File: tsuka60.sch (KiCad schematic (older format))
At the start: 165 parts, among them SW1 SW_Push, U1 ATmega32U4-AU, Y1 Resonator_Small

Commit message: completed all traces
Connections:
- net Col3: now also U1.31 (PC6); no longer U1.32 (PC7)
- net Col4: now also U1.32 (PC7); no longer U1.31 (PC6)
- net Row3: now also U1.29 (PB5); no longer U1.28 (PB4)
- net Row4: now also U1.28 (PB4); no longer U1.29 (PB5)
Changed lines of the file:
@@
 Text GLabel 5750 12050 2    50   Input ~ 0
 Row2
+Text GLabel 5750 10850 2    50   Input ~ 0
+Row3
 Text GLabel 5750 10750 2    50   Input ~ 0
-Row3
-Text GLabel 5750 10850 2    50   Input ~ 0
 Row4
 Text GLabel 5750 12750 2    50   Input ~ 0
@@
 Text GLabel 5750 12950 2    50   Input ~ 0
 Col2
+Text GLabel 5750 11250 2    50   Input ~ 0
+Col3
 Text GLabel 5750 11350 2    50   Input ~ 0
-Col3
-Text GLabel 5750 11250 2    50   Input ~ 0
 Col4
 Text GLabel 5750 13250 2    50   Input ~ 0

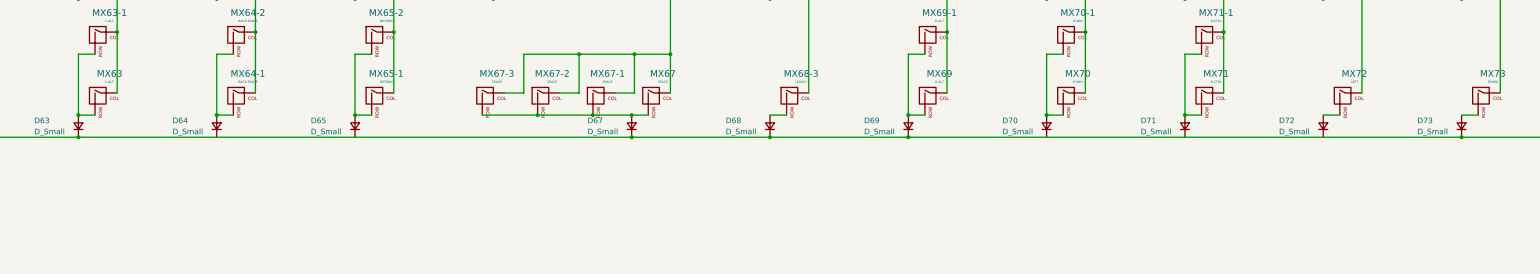
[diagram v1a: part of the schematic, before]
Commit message: Fixed broken traces
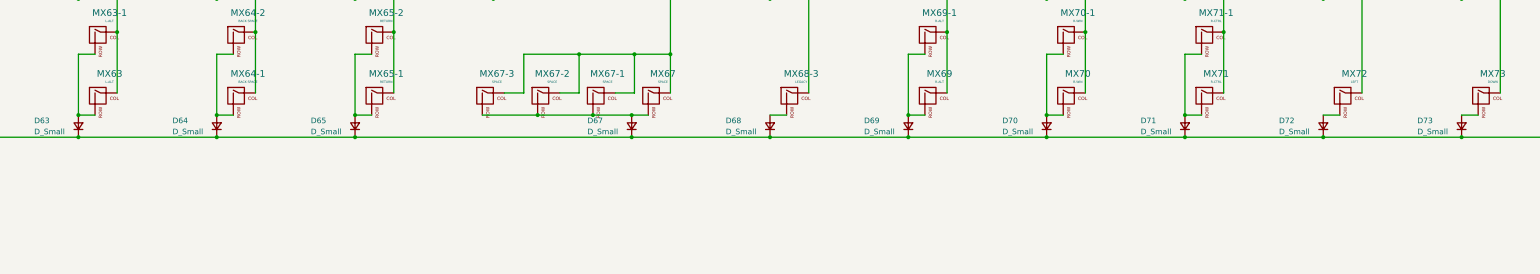
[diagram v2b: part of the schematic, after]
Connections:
- net Row4: now also D64.1 (K), D65.1 (K), D70.1 (K), D71.1 (K), D72.1 (K)
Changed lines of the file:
@@
 Wire Wire Line
 	18800 7300 18650 7300
-Wire Wire Line
-	18650 7500 19900 7500
 Connection ~ 18650 7500
 $Comp
@@
 	8650 6250 11150 6250
 Wire Wire Line
-	4900 7500 9900 7500
-Wire Wire Line
-	12400 7500 17400 7500
-Wire Wire Line
 	17750 5850 17750 7100
 Wire Wire Line
@@
 	16500 1250 16500 2100
 Connection ~ 16500 2100
+Wire Wire Line
+	4900 7500 6150 7500
+Connection ~ 6150 7500
+Wire Wire Line
+	6150 7500 7400 7500
+Connection ~ 7400 7500
+Wire Wire Line
+	7400 7500 9900 7500
+Wire Wire Line
+	18650 7500 19900 7500
+Wire Wire Line
+	12400 7500 13650 7500
+Connection ~ 13650 7500
+Wire Wire Line
+	13650 7500 14900 7500
+Connection ~ 16150 7500
+Wire Wire Line
+	16150 7500 17400 7500
+Connection ~ 14900 7500
+Wire Wire Line
+	14900 7500 16150 7500
 $EndSCHEMATC

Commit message: updated the schematic
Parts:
- removed D68: D_Small, Diode_SMD:D_0805_2012Metric, symbol Device:D_Small
- removed MX67-1: SPACE, MX_Alps_Hybrid:MX-2.75U-ReversedStabilizers-NoLED, symbol MX_Alps_Hybrid:MX-NoLED
- removed MX67-2: SPACE, MX_Alps_Hybrid:MX-3U-ReversedStabilizers-NoLED, symbol MX_Alps_Hybrid:MX-NoLED
- removed MX67-3: SPACE, MX_Alps_Hybrid:MX-6.25U-ReversedStabilizers-NoLED, symbol MX_Alps_Hybrid:MX-NoLED
- removed MX68-3: LEGACY, MX_Alps_Hybrid:MX-1.25U-NoLED, symbol MX_Alps_Hybrid:MX-NoLED
- added D37, D39, D52, D54, D66: D_Small, Diode_SMD:D_0805_2012Metric, symbol Device:D_Small
- added MX31-1: CAPS-SHORT, MX_Alps_Hybrid:MX-1.25U-NoLED, symbol MX_Alps_Hybrid:MX-NoLED
- added MX37: LEGACY-H, MX_Alps_Hybrid:MX-1U-NoLED, symbol MX_Alps_Hybrid:MX-NoLED
- added MX39: H, MX_Alps_Hybrid:MX-1.5U-NoLED, symbol MX_Alps_Hybrid:MX-NoLED
- added MX44-1: RETURN-SHORT, MX_Alps_Hybrid:MX-1.75U-NoLED, symbol MX_Alps_Hybrid:MX-NoLED
- added MX52: M1, MX_Alps_Hybrid:MX-1U-NoLED, symbol MX_Alps_Hybrid:MX-NoLED
- added MX54: M3, MX_Alps_Hybrid:MX-1U-NoLED, symbol MX_Alps_Hybrid:MX-NoLED
- added MX65-2: RETURN, MX_Alps_Hybrid:MX-1.5U-NoLED, symbol MX_Alps_Hybrid:MX-NoLED
- added MX65-3: SPACE, MX_Alps_Hybrid:MX-1.5U-NoLED, symbol MX_Alps_Hybrid:MX-NoLED
- added MX66-1, MX66-2: SPACE RIGHT, MX_Alps_Hybrid:MX-1.5U-NoLED, symbol MX_Alps_Hybrid:MX-NoLED
- MX1: value MX-LED -> ESC
- MX10: value MX-LED -> 7
- MX11: value MX-LED -> 8
- MX12: value MX-LED -> 9
- MX13: value MX-LED -> 10
- MX14: value MX-LED -> MINUS
- MX15: value MX-LED -> PLUS
- MX16: value MX-LED -> TAB 1
- MX17: value MX-LED -> TAB 2
- MX18: value MX-LED -> Q
- MX19: value MX-LED -> W
- MX2: value MX-LED -> TILDE
- MX20: value MX-LED -> E
- MX21: value MX-LED -> R
- MX22: value MX-LED -> T
- MX23: value MX-LED -> M4
- MX24: value MX-LED -> Y
- MX25: value MX-LED -> U
- MX26: value MX-LED -> I
- MX27: value MX-LED -> O
- MX28: value MX-LED -> P
- MX29: value MX-LED -> L-BRACKET
- MX3: value MX-LED -> 1
- MX30: value MX-LED -> R-BRACKET
- MX31: value MX-LED -> CAPS
- MX32: value MX-LED -> A
- MX33: value MX-LED -> S
- MX34: value MX-LED -> D
- MX35: value MX-LED -> F
- MX36: value MX-LED -> G
- MX38: value MX-LED -> BACKSPACE
- MX4: value MX-LED -> 2
- MX40: value MX-LED -> J
- MX41: value MX-LED -> K
- MX42: value MX-LED -> L
- MX43: value MX-LED -> SEMI-COLON
- MX44: value MX-LED -> RETURN
- MX45: value MX-LED -> BACKSPACE 2U
- MX46: value MX-LED -> L-SHIFT
- MX47: value MX-LED -> Z
- MX48: value MX-LED -> X
- MX49: value MX-LED -> C
- MX5: value MX-LED -> 3
- MX50: value MX-LED -> V
- MX51: value MX-LED -> B
- MX53: value MX-LED -> M2
- MX55: value MX-LED -> N
- MX56: value MX-LED -> M
- MX57: value MX-LED -> COMMA
- MX58: value MX-LED -> STOP
- MX59: value MX-LED -> SLASH
- MX6: value MX-LED -> 4
- MX60: value MX-LED -> R-SHIFT
- MX64-1, MX64-2: value BACK SPACE -> SPACE LEFT
- MX65: renamed from MX65-1; value RETURN -> SPACE
- MX67-3: renamed from MX67; value SPACE -> LEGACY-BOTTOM
- MX7: value MX-LED -> 5
- MX8: value MX-LED -> M5
- MX9: value MX-LED -> 6
- renumbered MX65-2 to MX65-1
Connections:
- net Col0: now also MX31-1.1 (COL)
- net Col13: now also MX44-1.1 (COL)
- net Col4: now also MX65-2.1 (COL), MX65-3.1 (COL)
- net Col5: now also MX66-1.1 (COL), MX66-2.1 (COL)
- net Col6: now also MX37.1 (COL), MX52.1 (COL)
- net Col8: now also MX39.1 (COL), MX54.1 (COL)
- net Row2: now also D37.1 (K), D39.1 (K)
- net Row3: now also D52.1 (K), D54.1 (K)
- net Row4: now also D66.1 (K)
- net at D65.2 (A), MX65-1.2 (ROW), MX65.2 (ROW): now also MX65-2.2 (ROW), MX65-3.2 (ROW)
- net at D31.2 (A), MX31.2 (ROW): now also MX31-1.2 (ROW)
- net at D44.2 (A), MX44.2 (ROW): now also MX44-1.2 (ROW)
- new net: D52.2 (A), MX52.2 (ROW)
- new net: D54.2 (A), MX54.2 (ROW)
- new net: D37.2 (A), MX37.2 (ROW)
- new net: D39.2 (A), MX39.2 (ROW)
- new net: D66.2 (A), MX66-1.2 (ROW), MX66-2.2 (ROW)
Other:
- moved on the sheet: MX65, MX65-1

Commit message: updated the routing
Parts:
- removed D37: D_Small, Diode_SMD:D_0805_2012Metric, symbol Device:D_Small
- MX39: footprint MX_Alps_Hybrid:MX-1.5U-NoLED -> MX_Alps_Hybrid:MX-1U-NoLED
- MX44: footprint MX_Alps_Hybrid:MX-1U-NoLED -> MX_Alps_Hybrid:MX-1.75U-NoLED
- MX44-1: footprint MX_Alps_Hybrid:MX-1.75U-NoLED -> MX_Alps_Hybrid:MX-1.25U-NoLED
- MX45: footprint MX_Alps_Hybrid:MX-1.75U-NoLED -> MX_Alps_Hybrid:MX-2U-NoLED
- MX65: footprint MX_Alps_Hybrid:MX-2U-ReversedStabilizers-NoLED -> MX_Alps_Hybrid:MX-7U-ReversedStabilizers-NoLED
- MX65-1: footprint MX_Alps_Hybrid:MX-1.5U-NoLED -> MX_Alps_Hybrid:MX-2U-ReversedStabilizers-NoLED
- MX65-3: footprint MX_Alps_Hybrid:MX-1.5U-NoLED -> MX_Alps_Hybrid:MX-6.25U-ReversedStabilizers-NoLED
- MX66-1: footprint MX_Alps_Hybrid:MX-1.5U-NoLED -> MX_Alps_Hybrid:MX-2.75U-ReversedStabilizers-NoLED
- MX66-2: footprint MX_Alps_Hybrid:MX-1.5U-NoLED -> MX_Alps_Hybrid:MX-3U-ReversedStabilizers-NoLED
- MX67-3: footprint MX_Alps_Hybrid:MX-7U-NoLED -> MX_Alps_Hybrid:MX-1.25U-NoLED
- renumbered MX72 to MX72-4, MX73 to MX73-4, MX74 to MX74-4, MX75 to MX75-4
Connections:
- net Col0: now also MX31-1.2 (ROW); no longer MX31-1.1 (COL)
- net Col1: now also U1.10 (PB2); no longer U1.40 (PF1)
- net Col13: now also MX44-1.2 (ROW); no longer MX44-1.1 (COL)
- net Col3: now also U1.38 (PF5); no longer U1.31 (PC6)
- net Col5: now also U1.31 (PC6); no longer U1.36 (PF7)
- net Col6: now also U1.30 (PB6); no longer MX37.1 (COL), U1.38 (PF5)
- net Col7: now also MX37.1 (COL), MX38.2 (ROW), U1.29 (PB5); no longer MX38.1 (COL), U1.37 (PF6)
- net Col8: now also U1.28 (PB4); no longer U1.30 (PB6)
- net Row0: now also U1.1 (PE6); no longer U1.8 (PB0)
- net Row1: now also U1.8 (PB0); no longer U1.1 (PE6)
- net Row2: now also U1.9 (PB1); no longer U1.22 (PD5)
- net Row3: now also U1.37 (PF6); no longer U1.29 (PB5)
- net Row4: now also U1.40 (PF1); no longer U1.28 (PB4)
- net at D31.2 (A), MX31.2 (ROW): now also MX31-1.1 (COL); no longer MX31-1.2 (ROW)
- net at D38.2 (A): now also MX37.2 (ROW), MX38.1 (COL); no longer MX38.2 (ROW)
- net at D44.2 (A), MX44.2 (ROW): now also MX44-1.1 (COL); no longer MX44-1.2 (ROW)
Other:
- moved on the sheet: C1, C2, C3, C4, C5, D61, D62, D63, D64, D65, D66, D67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

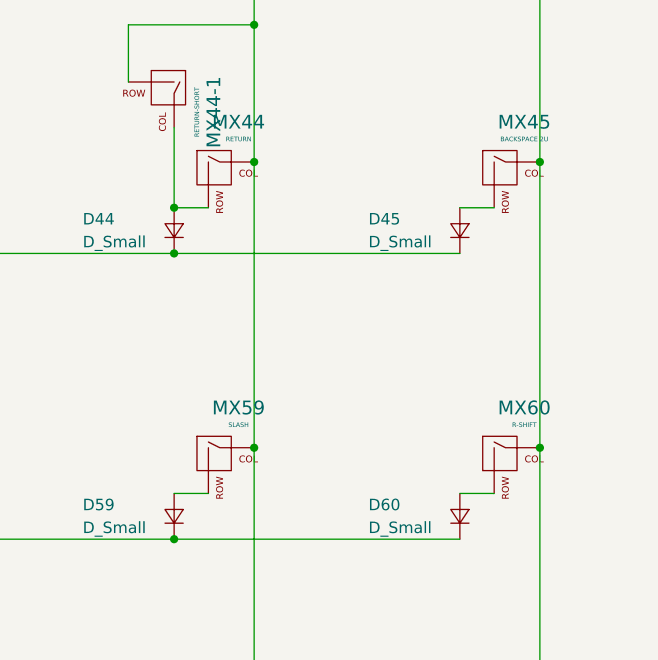
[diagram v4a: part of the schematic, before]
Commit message: Added alternative right-shift keys
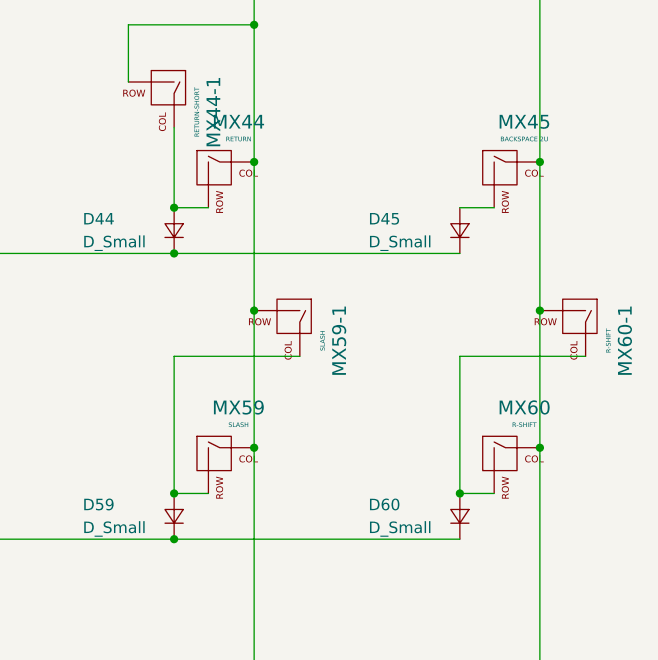
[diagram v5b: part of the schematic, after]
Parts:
- added MX59-1: SLASH, MX_Alps_Hybrid:MX-1.5U-NoLED, symbol MX_Alps_Hybrid:MX-NoLED
- added MX60-1: R-SHIFT, MX_Alps_Hybrid:MX-1U-NoLED, symbol MX_Alps_Hybrid:MX-NoLED
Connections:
- net Col13: now also MX59-1.2 (ROW)
- net Col14: now also MX60-1.2 (ROW)
- net at D59.2 (A), MX59.2 (ROW): now also MX59-1.1 (COL)
- net at D60.2 (A), MX60.2 (ROW): now also MX60-1.1 (COL)
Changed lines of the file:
@@
 Connection ~ 19000 4600
 Wire Wire Line
-	19000 4600 19000 5850
+	19000 4600 19000 5250
 Connection ~ 17750 4600
 Wire Wire Line
@@
 Connection ~ 20250 4600
 Wire Wire Line
-	20250 4600 20250 5850
+	20250 4600 20250 5250
 Connection ~ 20250 2100
 Connection ~ 20250 3350
@@
 Text GLabel 5325 14525 2    50   Input ~ 0
 Col0
+$Comp
+L MX_Alps_Hybrid:MX-NoLED MX59-1
+U 1 1 5EBC7D92
+P 19150 5300
+F 0 "MX59-1" H 19232 5524 60  0000 C CNN
+F 1 "SLASH" H 19232 5450 20  0000 C CNN
+F 2 "MX_Alps_Hybrid:MX-1.5U-NoLED" H 18525 5275 60  0001 C CNN
+F 3 "" H 18525 5275 60  0001 C CNN
+	1    19150 5300
+	0    1    1    0
+$EndComp
+Connection ~ 19000 5250
+Wire Wire Line
+	19000 5250 19000 5850
+$Comp
+L MX_Alps_Hybrid:MX-NoLED MX60-1
+U 1 1 5EBC9271
+P 20400 5300
+F 0 "MX60-1" H 20482 5524 60  0000 C CNN
+F 1 "R-SHIFT" H 20482 5450 20  0000 C CNN
+F 2 "MX_Alps_Hybrid:MX-1U-NoLED" H 19775 5275 60  0001 C CNN
+F 3 "" H 19775 5275 60  0001 C CNN
+	1    20400 5300
+	0    1    1    0
+$EndComp
+Connection ~ 20250 5250
+Wire Wire Line
+	20250 5250 20250 5850
+Wire Wire Line
+	20450 5450 19900 5450
+Wire Wire Line
+	19900 5450 19900 6050
+Connection ~ 19900 6050
+Wire Wire Line
+	19200 5450 18650 5450
+Wire Wire Line
+	18650 5450 18650 6050
+Connection ~ 18650 6050
 $EndSCHEMATC

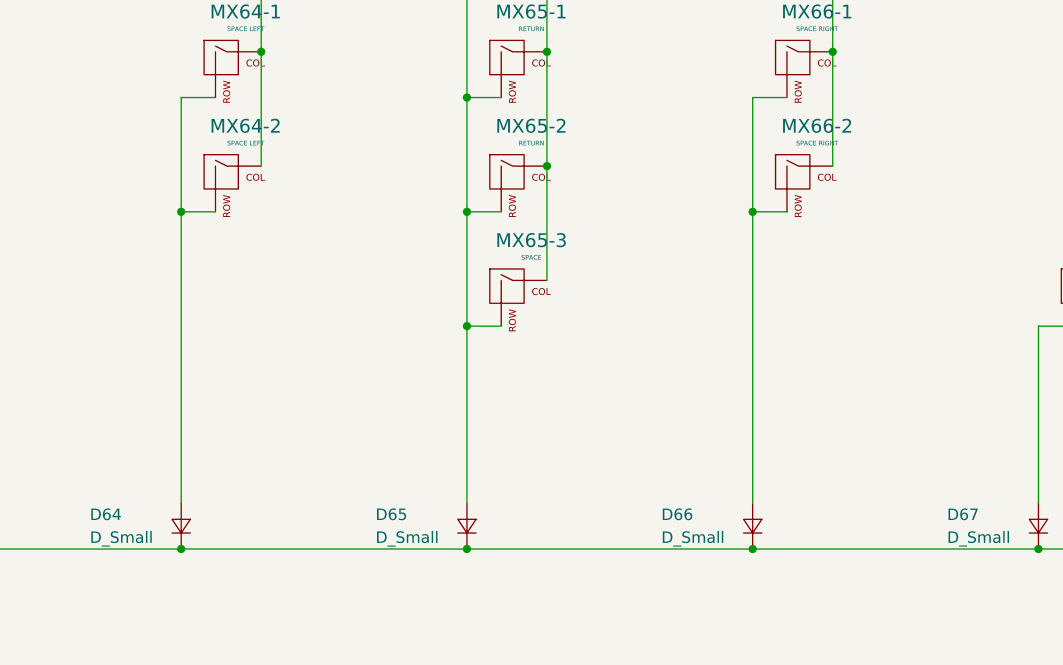
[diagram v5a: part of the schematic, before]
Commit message: added two new 2.75u footprints for ALPS compatibility
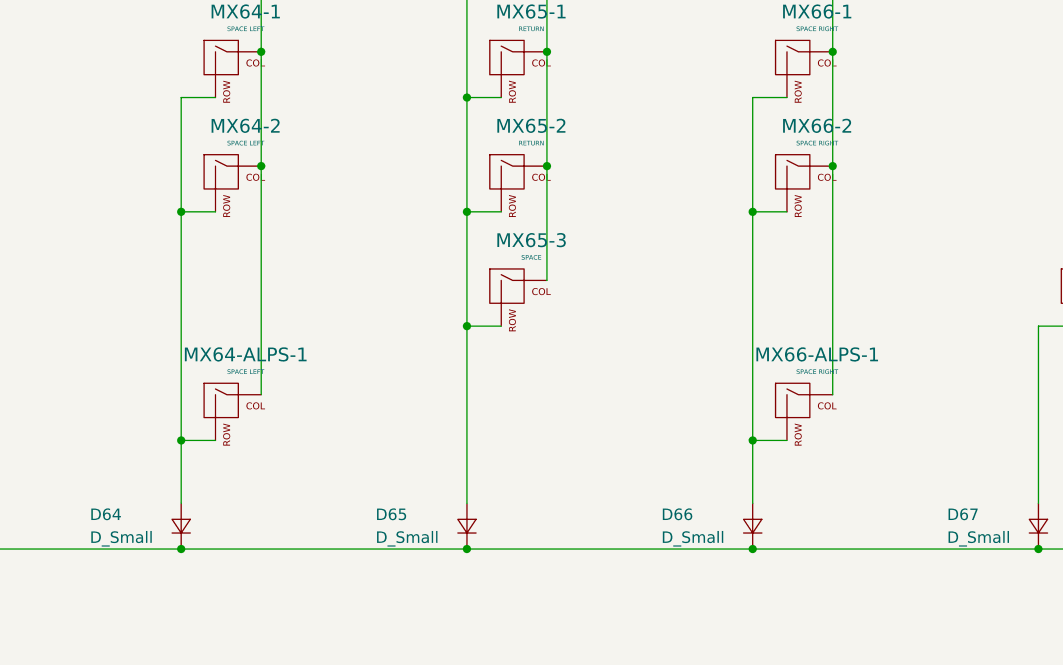
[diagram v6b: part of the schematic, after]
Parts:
- added MX64-ALPS-1: SPACE LEFT, MX_Alps_Hybrid:MX-2.75U-NoLED, symbol MX_Alps_Hybrid:MX-NoLED
- added MX66-ALPS-1: SPACE RIGHT, MX_Alps_Hybrid:MX-2.75U-NoLED, symbol MX_Alps_Hybrid:MX-NoLED
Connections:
- net Col3: now also MX64-ALPS-1.1 (COL)
- net Col5: now also MX66-ALPS-1.1 (COL)
- net at D64.2 (A), MX64-1.2 (ROW), MX64-2.2 (ROW): now also MX64-ALPS-1.2 (ROW)
- net at D66.2 (A), MX66-1.2 (ROW), MX66-2.2 (ROW): now also MX66-ALPS-1.2 (ROW)
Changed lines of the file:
@@
 	9900 8300 10050 8300
 Wire Wire Line
-	8650 9075 8650 7800
+	8650 9075 8650 8800
 Wire Wire Line
 	8650 7800 8800 7800
@@
 Connection ~ 6150 7800
 Wire Wire Line
-	6150 7800 6150 9075
+	6150 7800 6150 8800
 Connection ~ 5250 6600
 Wire Wire Line
@@
 	18650 5450 18650 6050
 Connection ~ 18650 6050
+$Comp
+L MX_Alps_Hybrid:MX-NoLED MX64-ALPS-1
+U 1 1 5E969378
+P 6350 8650
+F 0 "MX64-ALPS-1" H 6432 8874 60  0000 C CNN
+F 1 "SPACE LEFT" H 6432 8800 20  0000 C CNN
+F 2 "MX_Alps_Hybrid:MX-2.75U-NoLED" H 5725 8625 60  0001 C CNN
+F 3 "" H 5725 8625 60  0001 C CNN
+	1    6350 8650
+	1    0    0    -1
+$EndComp
+$Comp
+L MX_Alps_Hybrid:MX-NoLED MX66-ALPS-1
+U 1 1 5E96C8F7
+P 8850 8650
+F 0 "MX66-ALPS-1" H 8932 8874 60  0000 C CNN
+F 1 "SPACE RIGHT" H 8932 8800 20  0000 C CNN
+F 2 "MX_Alps_Hybrid:MX-2.75U-NoLED" H 8225 8625 60  0001 C CNN
+F 3 "" H 8225 8625 60  0001 C CNN
+	1    8850 8650
+	1    0    0    -1
+$EndComp
+Wire Wire Line
+	9000 7600 9000 8600
+Connection ~ 9000 7600
+Wire Wire Line
+	8800 8800 8650 8800
+Connection ~ 8650 8800
+Wire Wire Line
+	8650 8800 8650 7800
+Wire Wire Line
+	6500 8600 6500 7600
+Connection ~ 6500 7600
+Wire Wire Line
+	6300 8800 6150 8800
+Connection ~ 6150 8800
+Wire Wire Line
+	6150 8800 6150 9075
 $EndSCHEMATC
